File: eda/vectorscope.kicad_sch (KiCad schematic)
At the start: 58 parts, among them J1 PWR, J2 IO, J3 SCOPE, J4 SIGGEN, Q1 DMG2301L, SW1 SW_USER, SW10 SW_MENU, SW11 SW_LEVEL, SW12 SW_RANGE, SW13 SW_JOYSTICK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

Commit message: page templates
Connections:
- net GPIO0: now also U3.3 (CLK)
- net GPIO1: now also U3.2 (SDI)
- net GPIO16: now also U3.4 (~{LOAD})
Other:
- moved on the sheet: A1, C1, C15, C16, C17, C18, C19, C2, C20, C3, C4, J1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

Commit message: wrapped up schematic entry
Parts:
- added C10, C11, C13, C4: 100nF, symbol .stumbler:C
- added C12, C5, C6, C7, C8, C9: 2.2uF, symbol .stumbler:CAP
- added C2: 22uF, symbol .stumbler:CAP_POL
- added L1: 47uH, symbol .stumbler:L_Core_Iron
- added R8: 33R, symbol .stumbler:RES
- added ZD1: 3.0V, symbol Device:D_Zener
- J2: value IO -> IO CONNECTOR
- LS1: value Speaker -> SPEAKER
- renumbered A1 to XM1
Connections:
- net +3V3: now also U2.3 (TVDD), C4.1, C5.1, L1.1
- net +3V3F: now also U2.18 (AVDD), C10.1, C12.1, C13.1, C2.1, C9.1, L1.2, R8.2
- net GNDA: now also U2.20 (VREFL), C10.2, C11.2, C12.2, C13.2, C2.2, C6.2, C7.2, C8.2, C9.2, ZD1.2 (A)
- net GNDD: now also C4.2, C5.2
- net OUT3: no longer LY4.1 (K), U3.8 (OUT3)
- net OUT4: no longer LY5.1 (K), U3.9 (OUT4)
- net SW_~{USER}: now reaches R6.1, SW1.1, XM1.25 (GP19)
- net SIG_OUT3: now reaches U2.24 (AOUT2L), U3.3 (+)
- net SIG_OUT2: now reaches U2.23 (AOUT1R), U3.12 (+)
- net SIG_OUT4: now reaches U2.25 (AOUT2R), U3.5 (+)
- net SIG_OUT1: now reaches U2.22 (AOUT1L), U3.10 (+)
- net at U2.17 (VCOM): now also C7.1
- net at U2.5 (AVDRV): now also C6.1
- net GPIO0 renamed IO_CLK
- net GPIO1 renamed IO_SDI
- net GPIO10 renamed SDIN1
- net GPIO11 renamed SDIN2
- net GPIO12 renamed SDOUT1
- net GPIO13 renamed SDOUT2
- net GPIO16 renamed IO_~{LOAD}
- net GPIO2 renamed DISP_SCL
- net GPIO20 renamed COD_SDA
- net GPIO21 renamed COD_SCL
- net GPIO22 renamed SHUTUP
- net GPIO3 renamed DISP_SDA
- net GPIO4 renamed DISP_~{RST}
- net GPIO5 renamed DISP_D/~{C}
- net GPIO6 renamed PDN
- net GPIO7 renamed MCLK
- net GPIO8 renamed BICK
- net GPIO9 renamed LRCK
- net OUT0 renamed LED0
- net OUT1 renamed LED1
- net OUT10 renamed COL2
- net OUT11 renamed COL3
- net OUT12 renamed COL4
- net OUT13 renamed COL5
- net OUT14 renamed COL6
- net OUT15 renamed COL7
- net OUT2 renamed LED2
- net OUT5 renamed LED5
- net OUT6 renamed LED6
- net OUT7 renamed LED7
- net OUT8 renamed COL0
- net OUT9 renamed COL1
- new net: C11.1, C8.1, R8.1, U2.21 (VREFH), ZD1.1 (K)
- new net LED3: LY4.1 (K), U3.8 (OUT3)
- new net LED4: LY5.1 (K), U3.9 (OUT4)
- no-connect marks 1 -> 4
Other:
- note added: "CHRIS LOTT"
- note added: "REDRAWN BY:"
- company: (none) -> HACKADAY
- title: (none) -> \nVECTORSCOPE\nSUPERCON 2023
- moved on the sheet: C1, C15, C16, C17, C18, C19, C2, C20, C3, C4, J1, LS1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

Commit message: added pdf
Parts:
- added R1: 22, symbol .stumbler:RES
- added R12, R13: 2K7, symbol .stumbler:RES
- J1: value PWR -> EXT PWR
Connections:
- net +3V3: now also R12.1, R13.1
- net GNDD: now also U1.2 (LEDC)
- net SCL: now also R13.2
- net SDA: now also R12.2
- net at U1.3 (LEDA): now also R1.2
- net at U1.4 (V+): now also R1.1
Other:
- note added: "+3V3"
- note added: "AGND"
- note added: "DGND"
- note added: "USER INPUT SECTION"
- note removed: "INPUT SECTION"
- moved on the sheet: J1, XBT1, XBT2, XM1

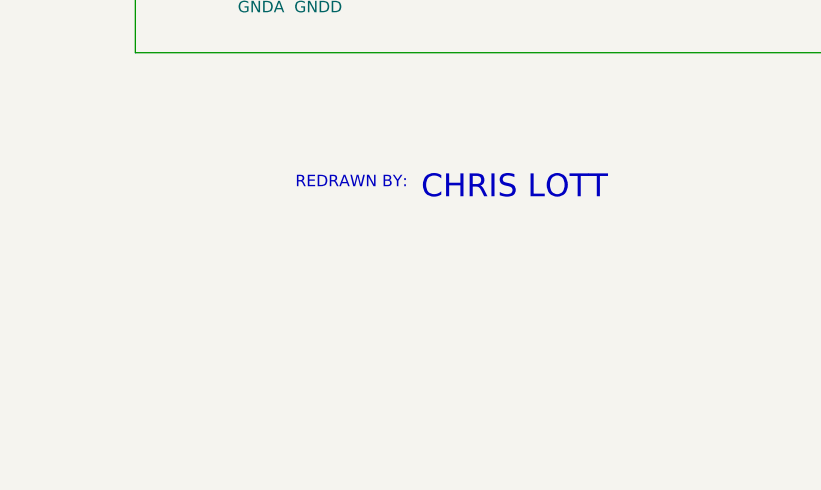
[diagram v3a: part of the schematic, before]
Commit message: added hackaday logo
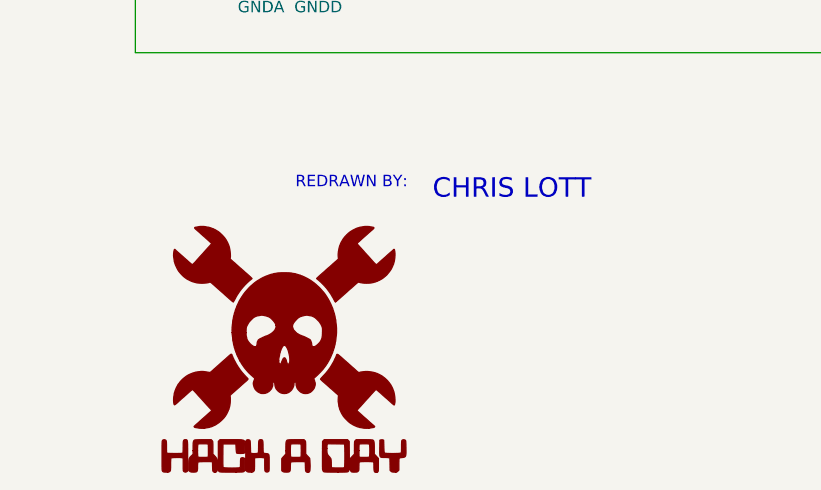
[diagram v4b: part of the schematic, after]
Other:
- company: HACKADAY -> (none)
- title: \nVECTORSCOPE\nSUPERCON 2023 -> \n\n    VECTORSCOPE\n  SUPERCON 2023
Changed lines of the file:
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@@
   (paper "A3")
   (title_block
-    (title "\\nVECTORSCOPE\\nSUPERCON 2023")
+    (title "\\n\\n    VECTORSCOPE\\n  SUPERCON 2023")
     (date "2023-11-08")
     (rev "-")
-    (company "HACKADAY")
     (comment 2 "SCHEMATICS")
   )
@@
     (fill (type none))
   )
-  (text "CHRIS LOTT" (at 280.67 255.27 0)
-    (effects (font (size 2.54 2.54)) (justify left bottom))
+  (text "CHRIS LOTT" (at 281.94 255.27 0)
+    (effects (font (size 2.159 2.159)) (justify left bottom))
   )
   (text "AGND" (at 382.27 149.86 0)
@@
     )
   )
+  (symbol (lib_id ".vector:HACKADAY_LOGO") (at 265.43 269.24 0) (unit 1)
+    (in_bom yes) (on_board yes) (dnp no) (fields_autoplaced)
+    (property "Reference" "#G1" (at 265.43 257.175 0)
+      (effects (font (size 1.27 1.27)) hide)
+    )
+    (property "Value" "HACKADAY_LOGO" (at 265.43 281.305 0)
+      (effects (font (size 1.27 1.27)) hide)
+    )
+    (property "Footprint" "" (at 265.43 269.24 0)
+      (effects (font (size 1.27 1.27)) hide)
+    )
+    (property "Datasheet" "" (at 265.43 269.24 0)
+      (effects (font (size 1.27 1.27)) hide)
+    )
+    (instances
+      (project "vectorscope"
+        (path "/179abe12-95b7-49b3-9fc0-c923203a6032"
+          (reference "#G1") (unit 1)
+        )
+      )
+    )
+  )
   (symbol (lib_id "Amplifier_Operational:LMV324") (at 354.33 157.48 0) (unit 1)
     (in_bom yes) (on_board yes) (dnp no)
@@
         )
       )
+    )
+  )
+  (symbol (lib_id ".vector:HACKADAY_TEXT") (at 266.065 283.845 0) (unit 1)
+    (in_bom yes) (on_board yes) (dnp no) (fields_autoplaced)
+    (property "Reference" "#G2" (at 266.065 279.4947 0)
+      (effects (font (size 1.27 1.27)) hide)
+    )
+    (property "Value" "LOGO" (at 266.065 288.1953 0)
+      (effects (font (size 1.27 1.27)) hide)
+    )
+    (property "Footprint" "" (at 266.065 283.845 0)
+      (effects (font (size 1.27 1.27)) hide)
+    )
+    (property "Datasheet" "" (at 266.065 283.845 0)
+      (effects (font (size 1.27 1.27)) hide)
+    )
+    (instances
+      (project "vectorscope"
+        (path "/179abe12-95b7-49b3-9fc0-c923203a6032"
+          (reference "#G2") (unit 1)
+        )
+      )

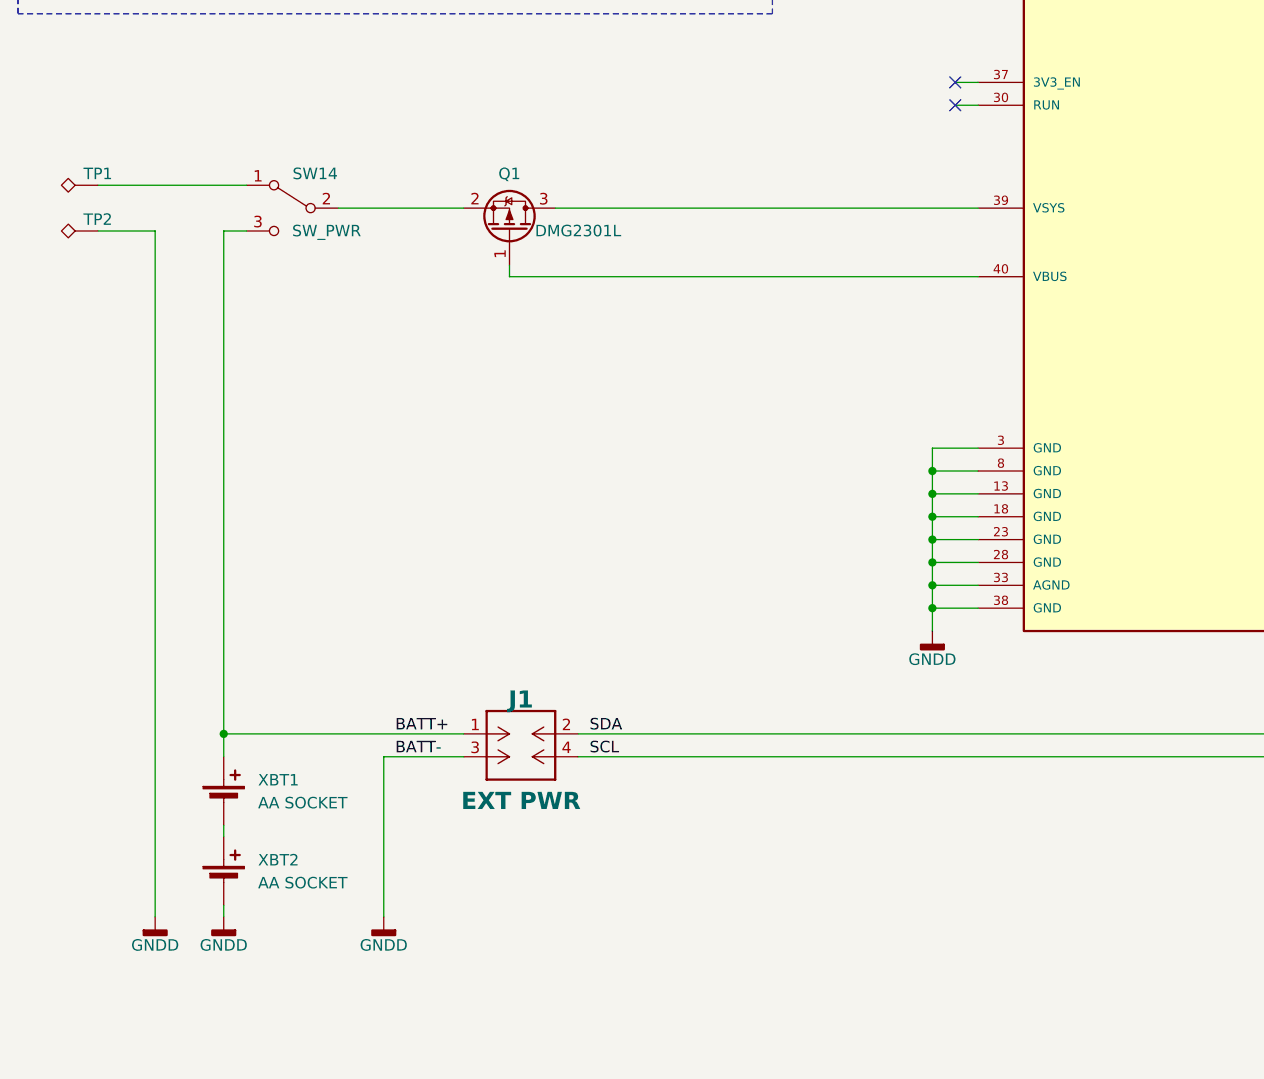
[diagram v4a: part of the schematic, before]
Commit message: added USB cable to Pico
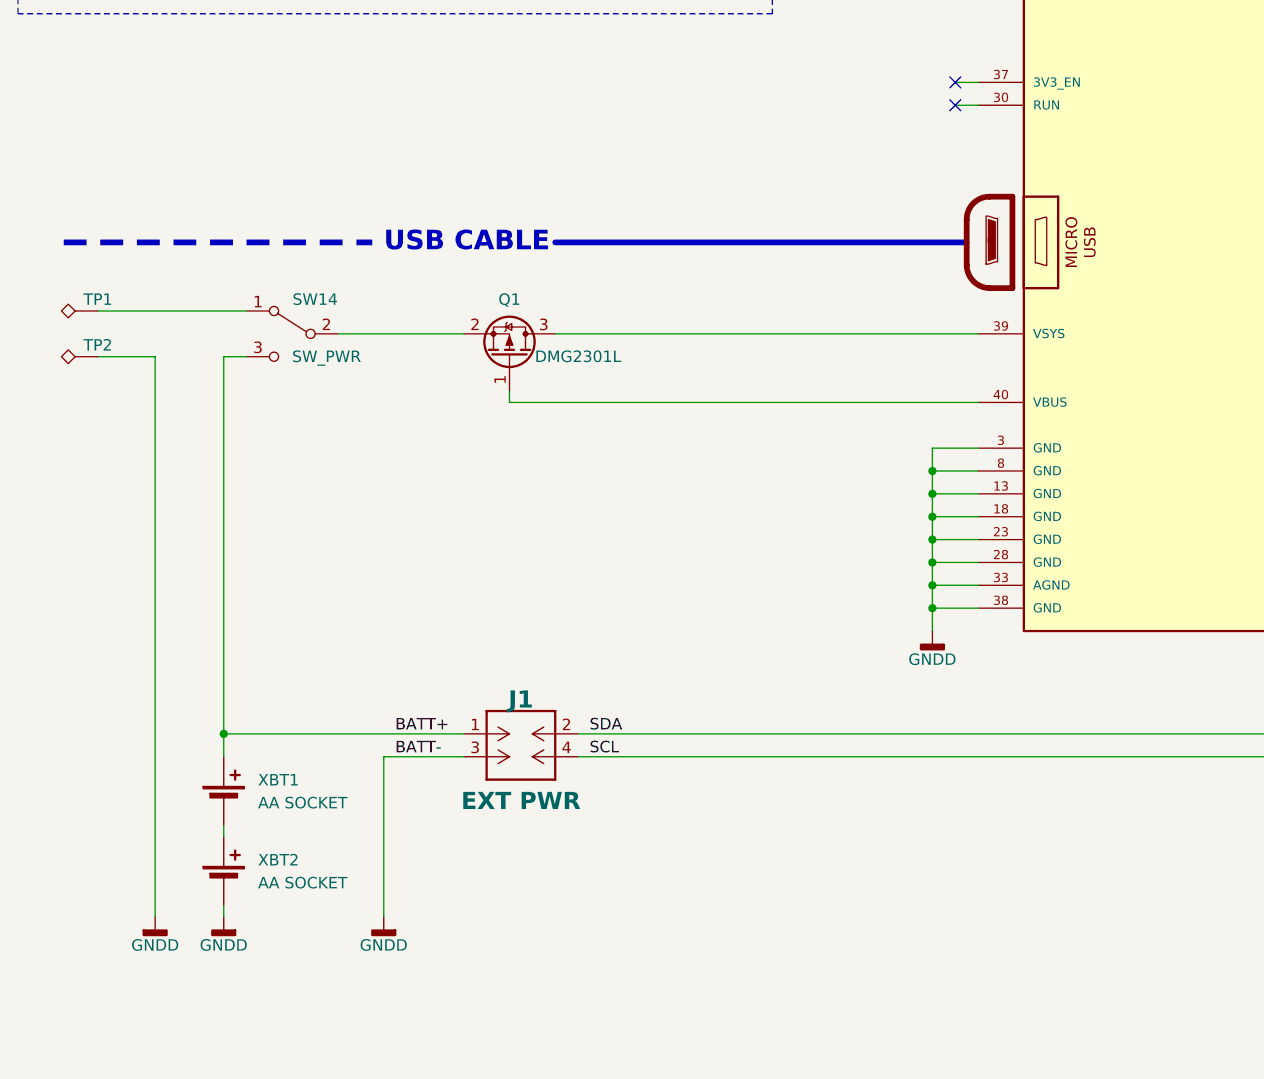
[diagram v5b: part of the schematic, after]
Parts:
- added P1: IO_PLUG_USB, symbol .vector:IO_PLUG_USB
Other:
- note added: "USB CABLE"
- moved on the sheet: Q1, SW14, TP1, TP2
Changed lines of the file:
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@@
     (stroke (width 0) (type default))
   )
-  (wire (pts (xy 90.17 189.23) (xy 90.17 187.96))
+  (wire (pts (xy 90.17 203.2) (xy 90.17 201.93))
     (stroke (width 0) (type default))
   )
@@
     (stroke (width 0) (type default))
   )
-  (wire (pts (xy 90.17 189.23) (xy 142.24 189.23))
+  (wire (pts (xy 90.17 203.2) (xy 142.24 203.2))
     (stroke (width 0) (type default))
   )
@@
     (stroke (width 0) (type default))
   )
-  (wire (pts (xy 58.42 184.15) (xy 58.42 240.03))
+  (wire (pts (xy 58.42 198.12) (xy 58.42 240.03))
     (stroke (width 0) (type default))
   )
@@
     (stroke (width 0) (type default))
   )
+  (polyline (pts (xy 95.25 185.42) (xy 140.97 185.42))
+    (stroke (width 0.635) (type default))
+  )
   (wire (pts (xy 157.48 41.91) (xy 147.32 41.91))
     (stroke (width 0) (type default))
@@
     (stroke (width 0) (type default))
   )
-  (wire (pts (xy 95.25 181.61) (xy 142.24 181.61))
+  (wire (pts (xy 95.25 195.58) (xy 142.24 195.58))
     (stroke (width 0) (type default))
   )
@@
     (stroke (width 0) (type default))
   )
-  (wire (pts (xy 71.12 181.61) (xy 85.09 181.61))
+  (wire (pts (xy 71.12 195.58) (xy 85.09 195.58))
     (stroke (width 0) (type default))
   )
@@
     (stroke (width 0) (type default))
   )
-  (wire (pts (xy 44.45 179.07) (xy 60.96 179.07))
+  (wire (pts (xy 44.45 193.04) (xy 60.96 193.04))
     (stroke (width 0) (type default))
   )
@@
     (stroke (width 0) (type default))
   )
-  (wire (pts (xy 50.8 184.15) (xy 50.8 260.35))
+  (wire (pts (xy 50.8 198.12) (xy 50.8 260.35))
     (stroke (width 0) (type default))
   )
@@
     (stroke (width 0) (type default))
   )
-  (wire (pts (xy 58.42 184.15) (xy 60.96 184.15))
+  (wire (pts (xy 58.42 198.12) (xy 60.96 198.12))
     (stroke (width 0) (type default))
   )
@@
     (stroke (width 0) (type default))
   )
+  (polyline (pts (xy 40.64 185.42) (xy 74.93 185.42))
+    (stroke (width 0.635) (type dash))
+  )
   (wire (pts (xy 66.04 132.08) (xy 69.85 132.08))
     (stroke (width 0) (type default))
@@
     (stroke (width 0) (type default))
   )
-  (wire (pts (xy 50.8 184.15) (xy 44.45 184.15))
+  (wire (pts (xy 50.8 198.12) (xy 44.45 198.12))
     (stroke (width 0) (type default))
   )
@@
     (effects (font (size 1.27 1.27)) (justify left bottom))
   )
+  (text "USB CABLE" (at 76.2 186.69 0)
+    (effects (font (size 2.159 2.159) (thickness 0.4318) bold) (justify left bottom))
+  )
   (text "REDRAWN BY:" (at 266.7 254 0)
     (effects (font (size 1.27 1.27)) (justify left bottom))
@@
     )
   )
-  (symbol (lib_id "Connector:TestPoint_Alt") (at 44.45 184.15 90) (unit 1)
+  (symbol (lib_id "Connector:TestPoint_Alt") (at 44.45 198.12 90) (unit 1)
     (in_bom yes) (on_board yes) (dnp no)
-    (property "Reference" "TP2" (at 44.45 182.88 90)
+    (property "Reference" "TP2" (at 44.45 196.85 90)
       (effects (font (size 1.27 1.27)))
     )
-    (property "Value" "TP_EXT_PAD" (at 41.148 181.61 90)
+    (property "Value" "TP_EXT_PAD" (at 41.148 195.58 90)
       (effects (font (size 1.27 1.27)) hide)
     )
-    (property "Footprint" "" (at 44.45 179.07 0)
+    (property "Footprint" "" (at 44.45 193.04 0)
       (effects (font (size 1.27 1.27)) hide)
     )
-    (property "Datasheet" "~" (at 44.45 179.07 0)
+    (property "Datasheet" "~" (at 44.45 193.04 0)
       (effects (font (size 1.27 1.27)) hide)
     )
@@
     )
   )
-  (symbol (lib_id ".vector:DMG2301L") (at 90.17 184.15 270) (mirror x) (unit 1)
+  (symbol (lib_id ".vector:DMG2301L") (at 90.17 198.12 270) (mirror x) (unit 1)
     (in_bom yes) (on_board yes) (dnp no)
-    (property "Reference" "Q1" (at 90.17 177.8 90)
+    (property "Reference" "Q1" (at 90.17 191.77 90)
       (effects (font (size 1.27 1.27)))
     )
-    (property "Value" "DMG2301L" (at 97.79 184.15 90)
+    (property "Value" "DMG2301L" (at 97.79 198.12 90)
       (effects (font (size 1.27 1.27)))
     )
-    (property "Footprint" "Package_TO_SOT_SMD:SOT-23" (at 88.265 179.07 0)
+    (property "Footprint" "Package_TO_SOT_SMD:SOT-23" (at 88.265 193.04 0)
       (effects (font (size 1.27 1.27) italic) (justify left) hide)
     )
-    (property "Datasheet" "https://www.diodes.com/assets/Datasheets/DMG2301L.pdf" (at 90.17 184.15 0)
+    (property "Datasheet" "https://www.diodes.com/assets/Datasheets/DMG2301L.pdf" (at 90.17 198.12 0)
       (effects (font (size 1.27 1.27)) (justify left) hide)
     )
@@
     )
   )
+  (symbol (lib_id ".vector:IO_PLUG_USB") (at 146.05 185.42 0) (mirror y) (unit 1)
+    (in_bom yes) (on_board yes) (dnp no)
+    (property "Reference" "P1" (at 137.16 181.61 0)
+      (effects (font (size 1.27 1.27)) (justify right) hide)
+    )
+    (property "Value" "IO_PLUG_USB" (at 129.54 190.5 0)
+      (effects (font (size 1.27 1.27)) (justify right) hide)
+    )
+    (property "Footprint" "" (at 148.59 185.42 0)
+      (effects (font (size 1.27 1.27)) hide)
+    )
+    (property "Datasheet" "" (at 148.59 185.42 0)
+      (effects (font (size 1.27 1.27)) hide)
+    )
+    (property "Sim.Enable" "0" (at 146.05 185.42 0)
+      (effects (font (size 1.27 1.27)) hide)
+    )
+    (instances
+      (project "vectorscope"
+        (path "/179abe12-95b7-49b3-9fc0-c923203a6032"
+          (reference "P1") (unit 1)
+        )
+      )
+    )
+  )
   (symbol (lib_id ".stumbler:+3V3F") (at 384.81 198.12 0) (unit 1)
     (in_bom yes) (on_board yes) (dnp no) (fields_autoplaced)
@@
     )
   )
-  (symbol (lib_id ".vector:SW_SPDT_SLIDE") (at 66.04 181.61 0) (mirror y) (unit 1)
+  (symbol (lib_id ".vector:SW_SPDT_SLIDE") (at 66.04 195.58 0) (mirror y) (unit 1)
     (in_bom yes) (on_board yes) (dnp no)
-    (property "Reference" "SW14" (at 68.58 177.8 0)
+    (property "Reference" "SW14" (at 68.58 191.77 0)
       (effects (font (size 1.27 1.27)))
     )
-    (property "Value" "SW_PWR" (at 69.85 184.15 0)
+    (property "Value" "SW_PWR" (at 69.85 198.12 0)
       (effects (font (size 1.27 1.27)))
     )
-    (property "Footprint" "" (at 66.04 181.61 0)
+    (property "Footprint" "" (at 66.04 195.58 0)
       (effects (font (size 1.27 1.27)) hide)
     )
-    (property "Datasheet" "~" (at 66.04 181.61 0)
+    (property "Datasheet" "~" (at 66.04 195.58 0)
       (effects (font (size 1.27 1.27)) hide)
     )
@@
     )
   )
-  (symbol (lib_id "Connector:TestPoint_Alt") (at 44.45 179.07 90) (unit 1)
+  (symbol (lib_id "Connector:TestPoint_Alt") (at 44.45 193.04 90) (unit 1)
     (in_bom yes) (on_board yes) (dnp no)
-    (property "Reference" "TP1" (at 44.45 177.8 90)
+    (property "Reference" "TP1" (at 44.45 191.77 90)
       (effects (font (size 1.27 1.27)))
     )
-    (property "Value" "TP_EXT_PAD" (at 41.148 176.53 90)
+    (property "Value" "TP_EXT_PAD" (at 41.148 190.5 90)
       (effects (font (size 1.27 1.27)) hide)
     )
-    (property "Footprint" "" (at 44.45 173.99 0)
+    (property "Footprint" "" (at 44.45 187.96 0)
       (effects (font (size 1.27 1.27)) hide)
     )
-    (property "Datasheet" "~" (at 44.45 173.99 0)
+    (property "Datasheet" "~" (at 44.45 187.96 0)
       (effects (font (size 1.27 1.27)) hide)
     )

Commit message: edited readme
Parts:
- SW1: value SW_USER -> USER
- SW10: value SW_MENU -> MENU
- SW11: value SW_LEVEL -> LEVEL
- SW12: value SW_RANGE -> RANGE
- SW13: value SW_JOYSTICK -> JOYSTICK
- SW14: value SW_PWR -> PWR
- SW2: value SW_SAVE -> SAVE
- SW7: value SW_XY -> XY
- SW8: value SW_WAVE -> WAVE
- SW9: value SW_SEL -> SEL
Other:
- moved on the sheet: C17, C18, C19, C2, C20, C4, R2, R3, R4
